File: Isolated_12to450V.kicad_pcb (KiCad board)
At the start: 4 copper layers, 85 x 47.5 mm, 93 parts, among them J1 Screw_Terminal_01x04, J20 T44007, J21 T44007, Q1 HY1707, Q20 BC817, Q21 SUD50P06-15, Q22 BC857, U1 UC3845, U20 TCMT1108, U21 TL431M

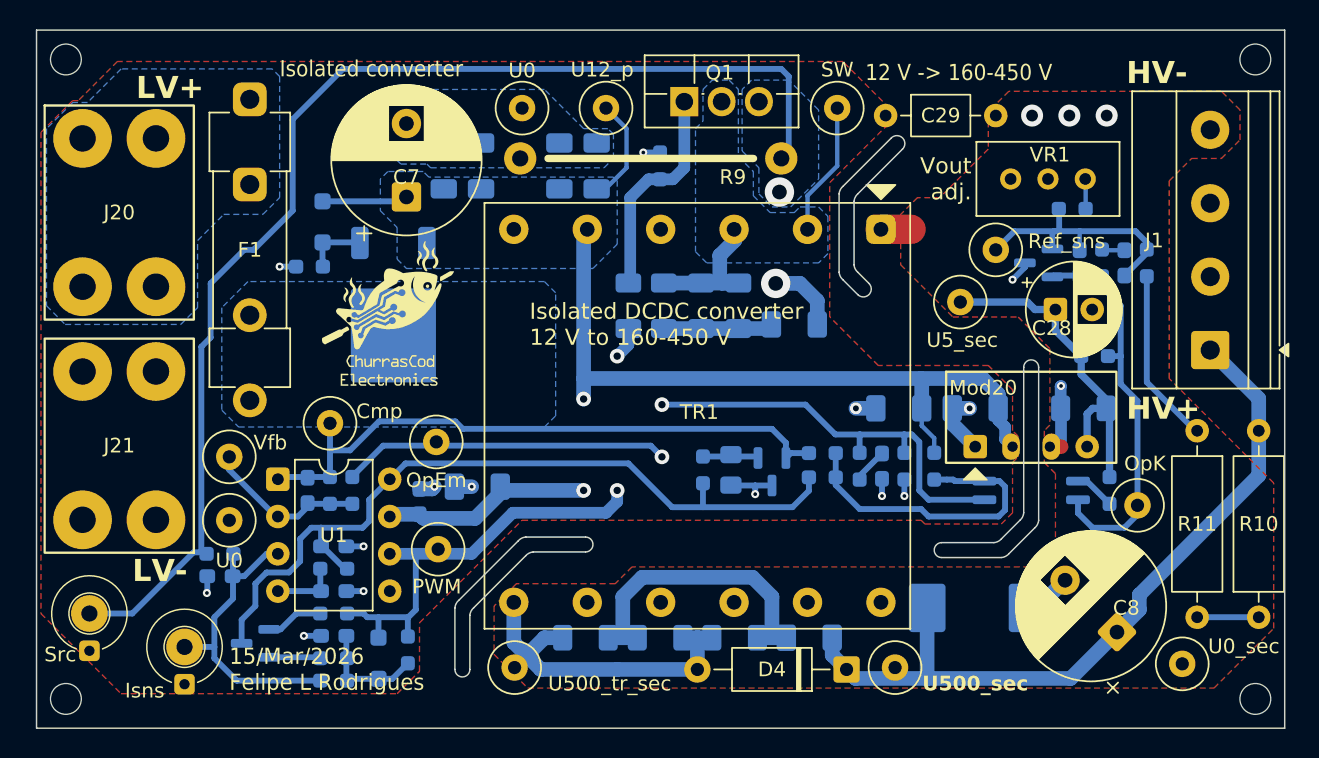
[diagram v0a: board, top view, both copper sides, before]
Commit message: Added power on LED
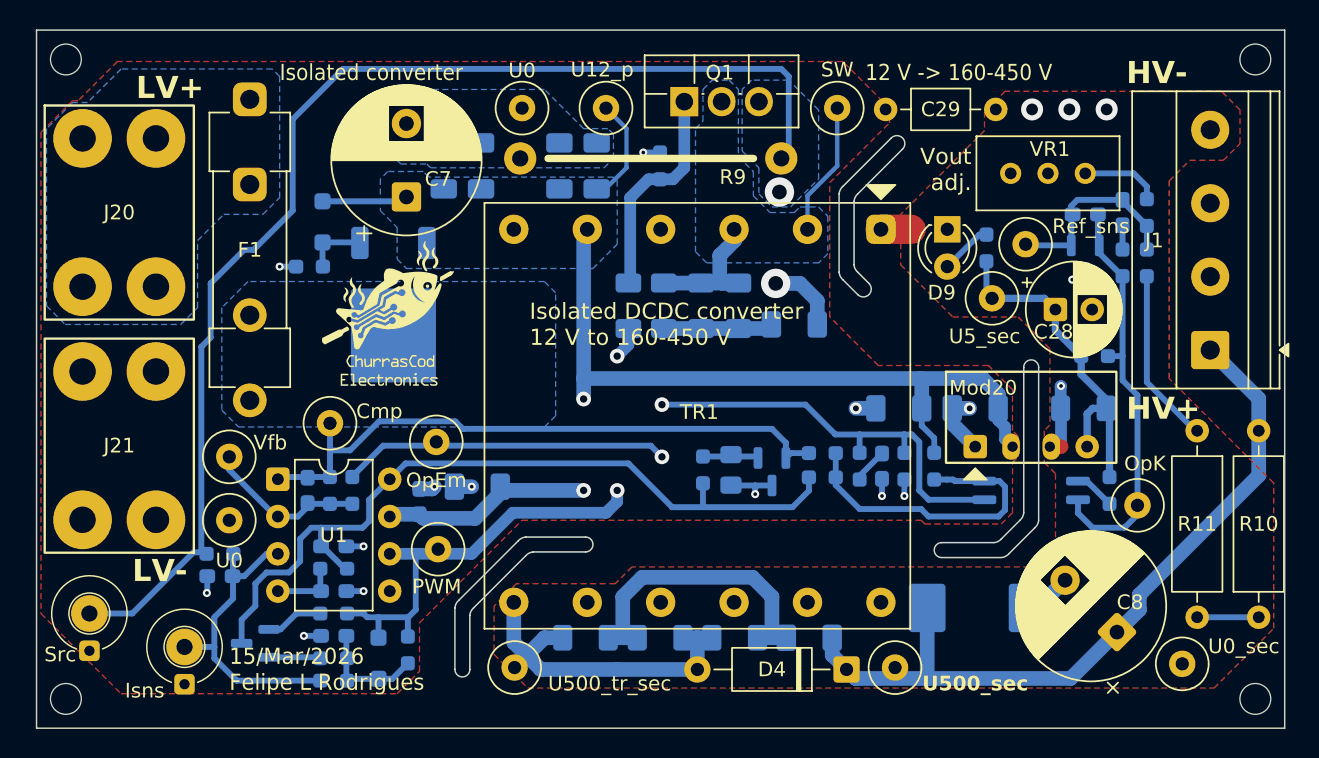
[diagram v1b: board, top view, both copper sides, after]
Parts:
- added D9: LED, LED_THT:LED_D3.0mm, F.Cu at (168.0, 54.9)
- added R13: 1k, Resistor_SMD:R_0603_1608Metric_Pad0.98x0.95mm_HandSolder, B.Cu at (170.7, 54.9)
- moved R4 5.09 mm to (181.6, 52.5), turned to 90 degrees
- moved C20 3.43 mm to (180.0, 52.5), turned to -90 degrees
- moved C21 3.32 mm to (177.4, 52.6), turned to 0 degrees
- moved U21 3.19 mm to (177.4, 55.6), turned to -90 degrees
- moved TP34 2.17 mm to (171.1, 58.3)
- moved TP9 2.07 mm to (173.4, 54.6)
- moved R20 1.40 mm to (180.0, 55.9)
- moved C29 0.42 mm to (163.8, 45.4)
- moved VR1 0.38 mm to (172.3, 49.8)
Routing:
- net /Block Diagram/Schematic/Sec_ref_sns: track 18.5 -> 13.8 mm
- net /Block Diagram/Schematic/LED_A_sec: track 0.00 -> 3.57 mm
- net /Block Diagram/Schematic/Sec_div_l: track 2.04 -> 5.46 mm
- net /Block Diagram/Schematic/Sec_OpK: track 27.3 -> 28.3 mm
- net /Block Diagram/Schematic/U5_sec: track 23.4 -> 24.0 mm
